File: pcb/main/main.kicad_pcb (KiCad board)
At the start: 2 copper layers, 48 x 48 mm, 33 parts, among them J1 Panel 1, J2 Panel 2, J3 Panel 3, J4 Panel 4, J5 Interboard, J6 Debug, SW1 SW_Push, U2 STM32L4A6RGTx, Y1 48MHz

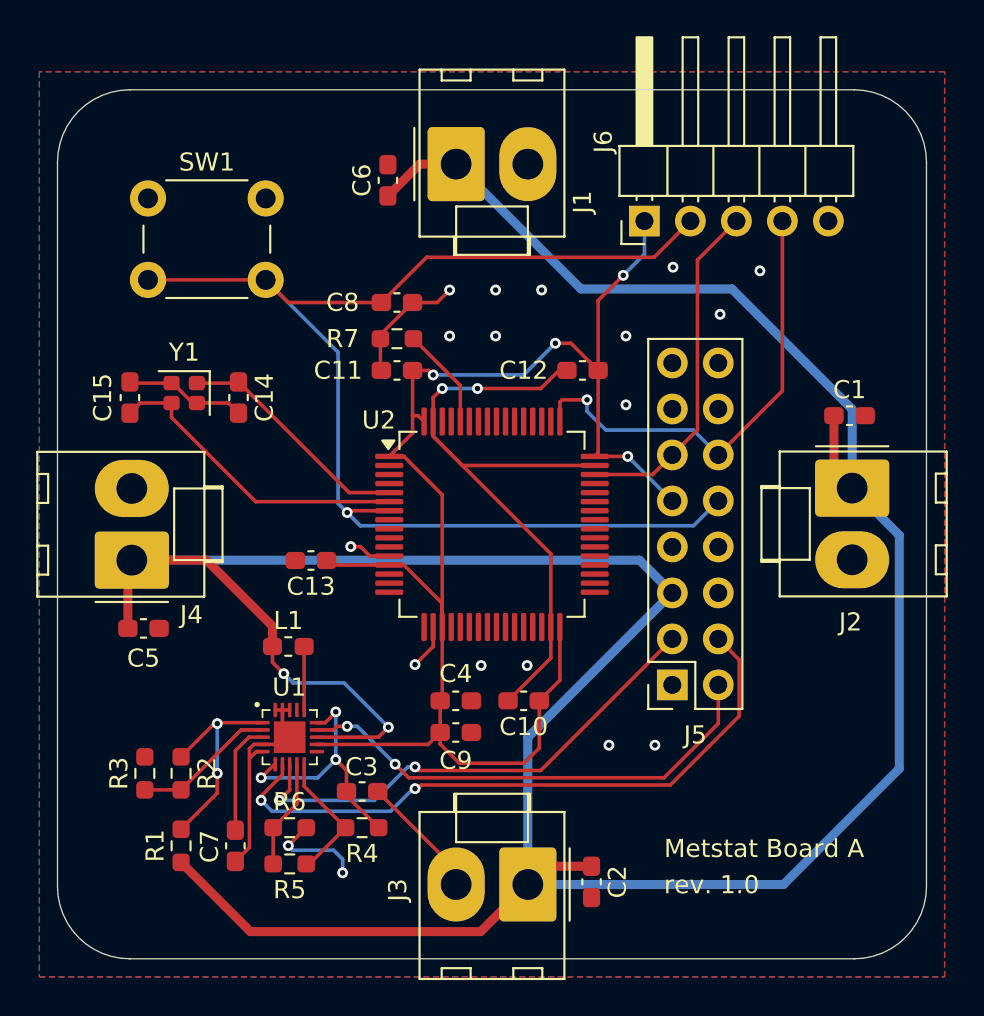
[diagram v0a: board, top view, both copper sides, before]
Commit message: pcb: add mounting holes, move debug connector
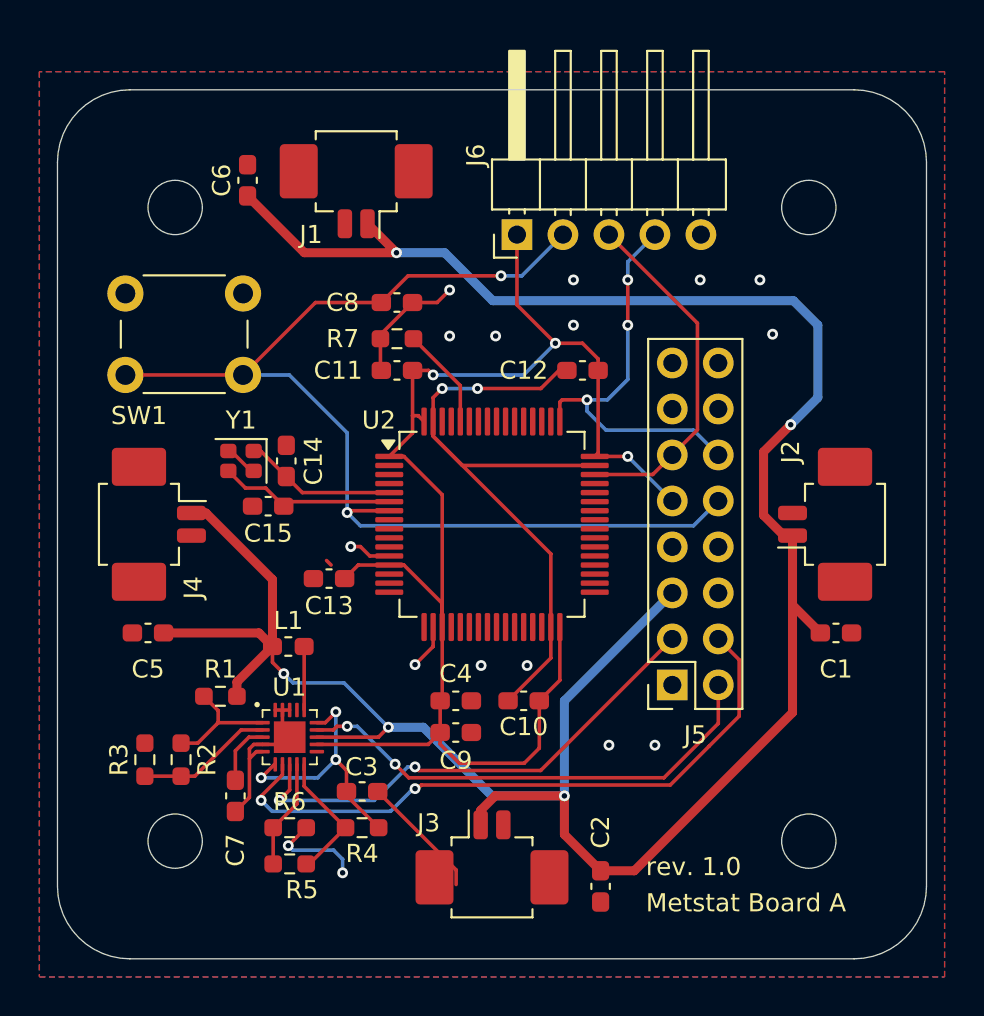
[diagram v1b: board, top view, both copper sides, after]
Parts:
- J1, J2, J3, J4: footprint Connector_Molex:Molex_KK-396_A-41791-0002_1x02_P3.96mm_Vertical -> Connector_Molex:Molex_PicoBlade_53261-0271_1x02-1MP_P1.25mm_Horizontal
- moved C1 12.0 mm to (169.0, 106.0)
- moved C15 9.71 mm to (137.6, 99.0), turned to 180 degrees
- moved R1 8.54 mm to (135.0, 109.5), turned to 180 degrees
- moved C6 7.75 mm to (136.5, 81.0)
- moved J6 7.08 mm to (151.4, 84.0)
- moved J1 5.59 mm to (142.5, 81.0), turned to 180 degrees
- moved SW1 5.40 mm to (129.8, 87.2)
- moved Y1 4.89 mm to (136.1, 96.5)
- moved C14 4.38 mm to (138.6, 96.5), turned to 90 degrees
- moved C7 2.76 mm to (135.8, 115.0)
- moved J2 2.19 mm to (169.0, 100.0), turned to 90 degrees
- moved J4 2.17 mm to (131.0, 100.0), turned to -90 degrees
- moved J3 2.17 mm to (150.0, 119.0), turned to 0 degrees
- moved C13 1.41 mm to (141.0, 103.0)
- moved R2 0.76 mm to (132.8, 113.0)
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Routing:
- net SOL: track 183.5 -> 144.9 mm, vias 2 -> 5
- net NRST: track 70.8 -> 62.6 mm, vias 1 -> 2
- net GND: track 81.2 -> 73.6 mm, vias 20 -> 18
- net /MCU/OSC_OUT: track 17.3 -> 9.80 mm
- net Net-(U1-MPP): track 11.9 -> 6.75 mm, vias 2 -> 0
- net /MCU/OSC_IN: track 13.2 -> 8.44 mm
- net SWCLK: track 25.9 -> 22.8 mm, vias 1 -> 3
- net Net-(U1-MPP_REF): track 6.20 -> 3.44 mm
- net +3V3: track 84.0 -> 81.5 mm, vias 4 -> 3
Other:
- outline, holes or cut-outs redrawn
